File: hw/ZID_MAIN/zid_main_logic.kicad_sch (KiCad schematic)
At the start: 84 parts, among them J1 Conn_01x02_Pin_2.54mm, J2 Conn_02x05_2.54mm, J3 Conn_02x05_2.54mm, J4 Conn_02x05_PINHDR_2.54mm, J5 HDR 1x04 Socket, J6 Conn_02x03_Odd_Even, J7 Conn_01x03, M1 WS-RP2040-Zero, SW1 SW_Push, SW2 SW_DIP_x02, U1 74HCT161, U10 74FCT2245, U11 SST39SF010, U12 AS7C1024B-10J, U13 74FCT541C, U14 74AHCT244, U15 74FCT257T, U16 74HCT166, U17 74HCT166, U18 74LVC245, U19 74LVC125AS, U2 74FCT541C, U20 24LC32, U21 ATF1504AS-44T, U22 74AHCT1G125, U23 74LVC273, U25 74LVC2G04, U26 74AHCT1G14, U3 74FCT541C, U4 MIC2775, U5 OSC-20MHz, U6 Z80 C20MHz-PLCC, U7 ATF1508AS, U8 74FCT2245, U9 74FCT2245

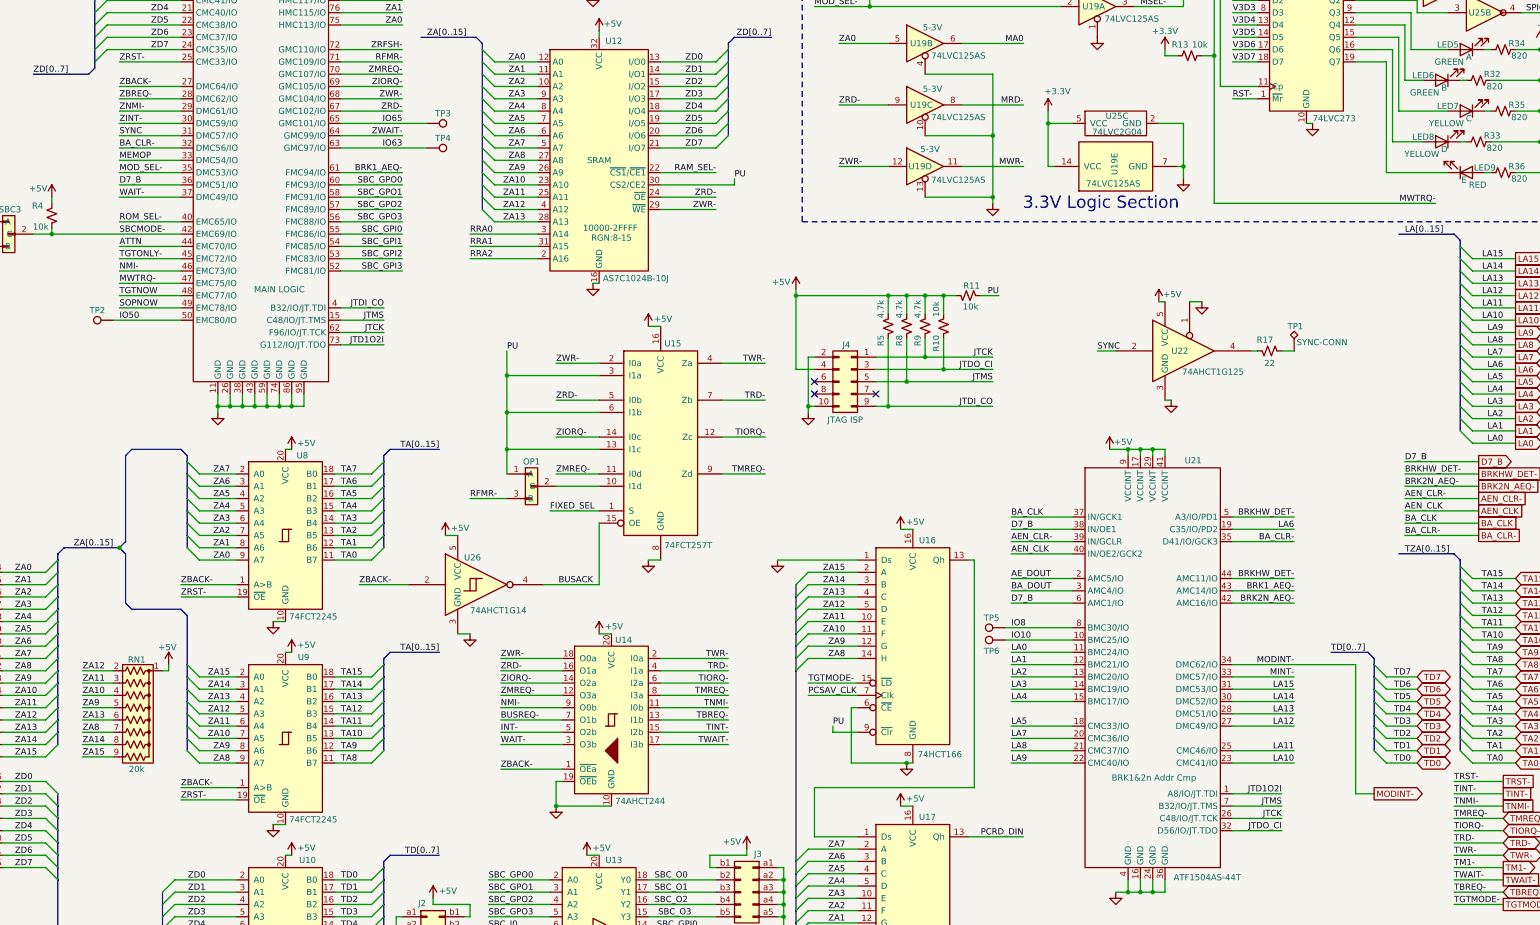
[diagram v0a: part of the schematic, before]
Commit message: BP-EXP: 1 board only. PLCC-DIP: Adapter form.
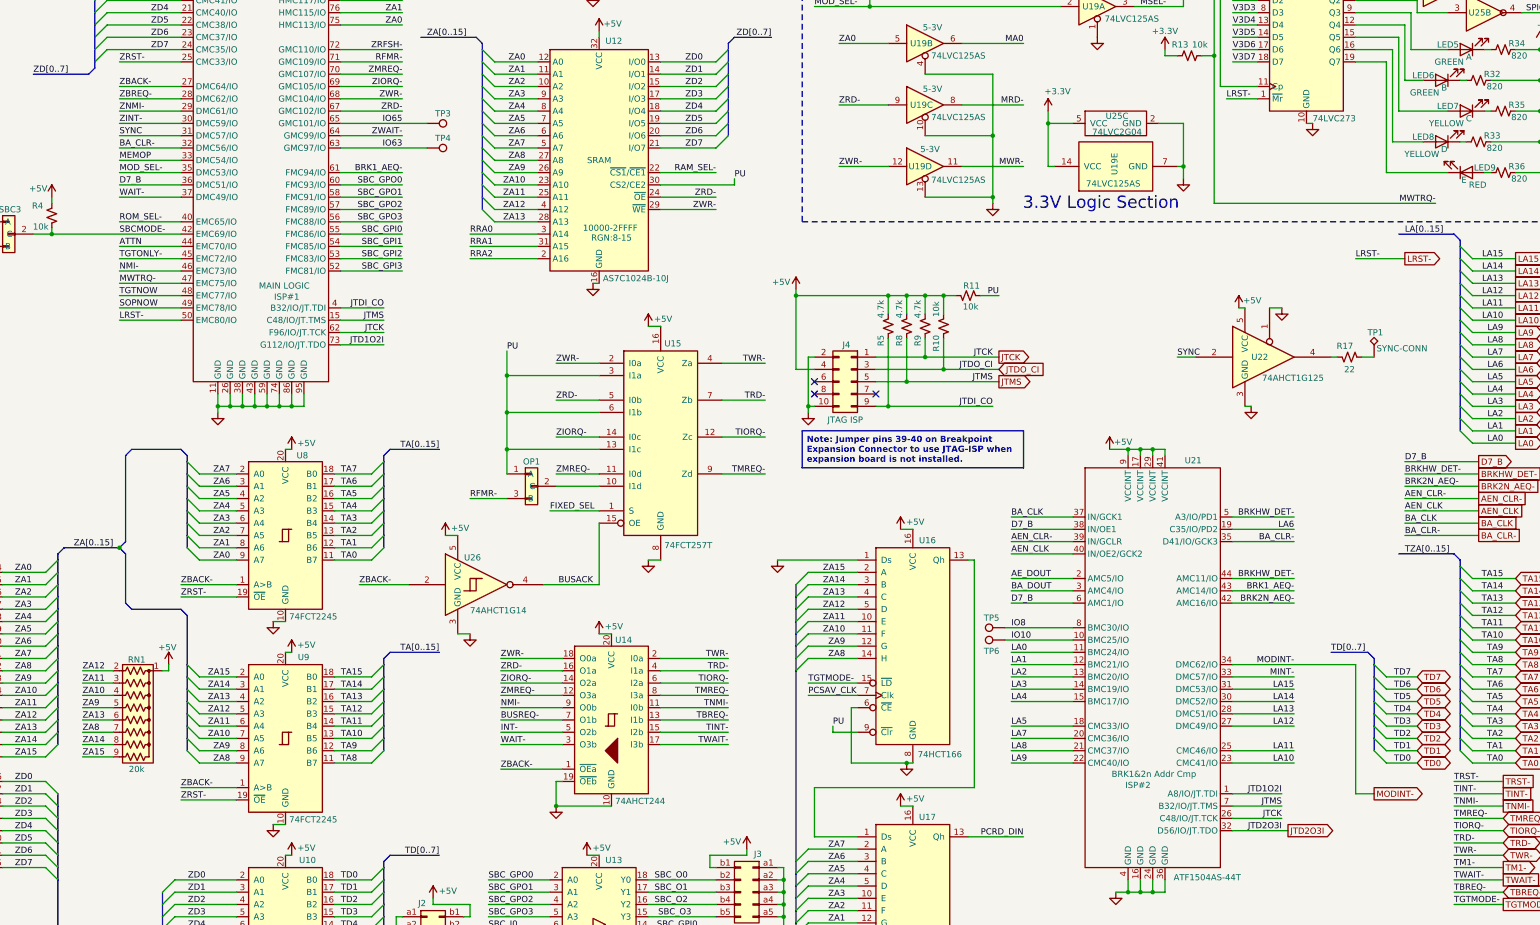
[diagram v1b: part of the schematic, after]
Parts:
- removed TP2: TestPoint, Connector_PinHeader_2.54mm:PinHeader_1x01_P2.54mm_Vertical, symbol Connector:TestPoint
- U21: ISP_CN (none) -> ISP#2
- U7: ISP_CN (none) -> ISP#1
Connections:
- net JTDO_CI: no longer U21.32 (D56/IO/JT.TDO)
- net RST-: no longer U23.1 (~{Mr})
- net IO50 renamed LRST-
- net LRST-: now also U23.1 (~{Mr})
- new net JTD2O3I: U21.32 (D56/IO/JT.TDO)
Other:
- moved on the sheet: R17, TP1, U22

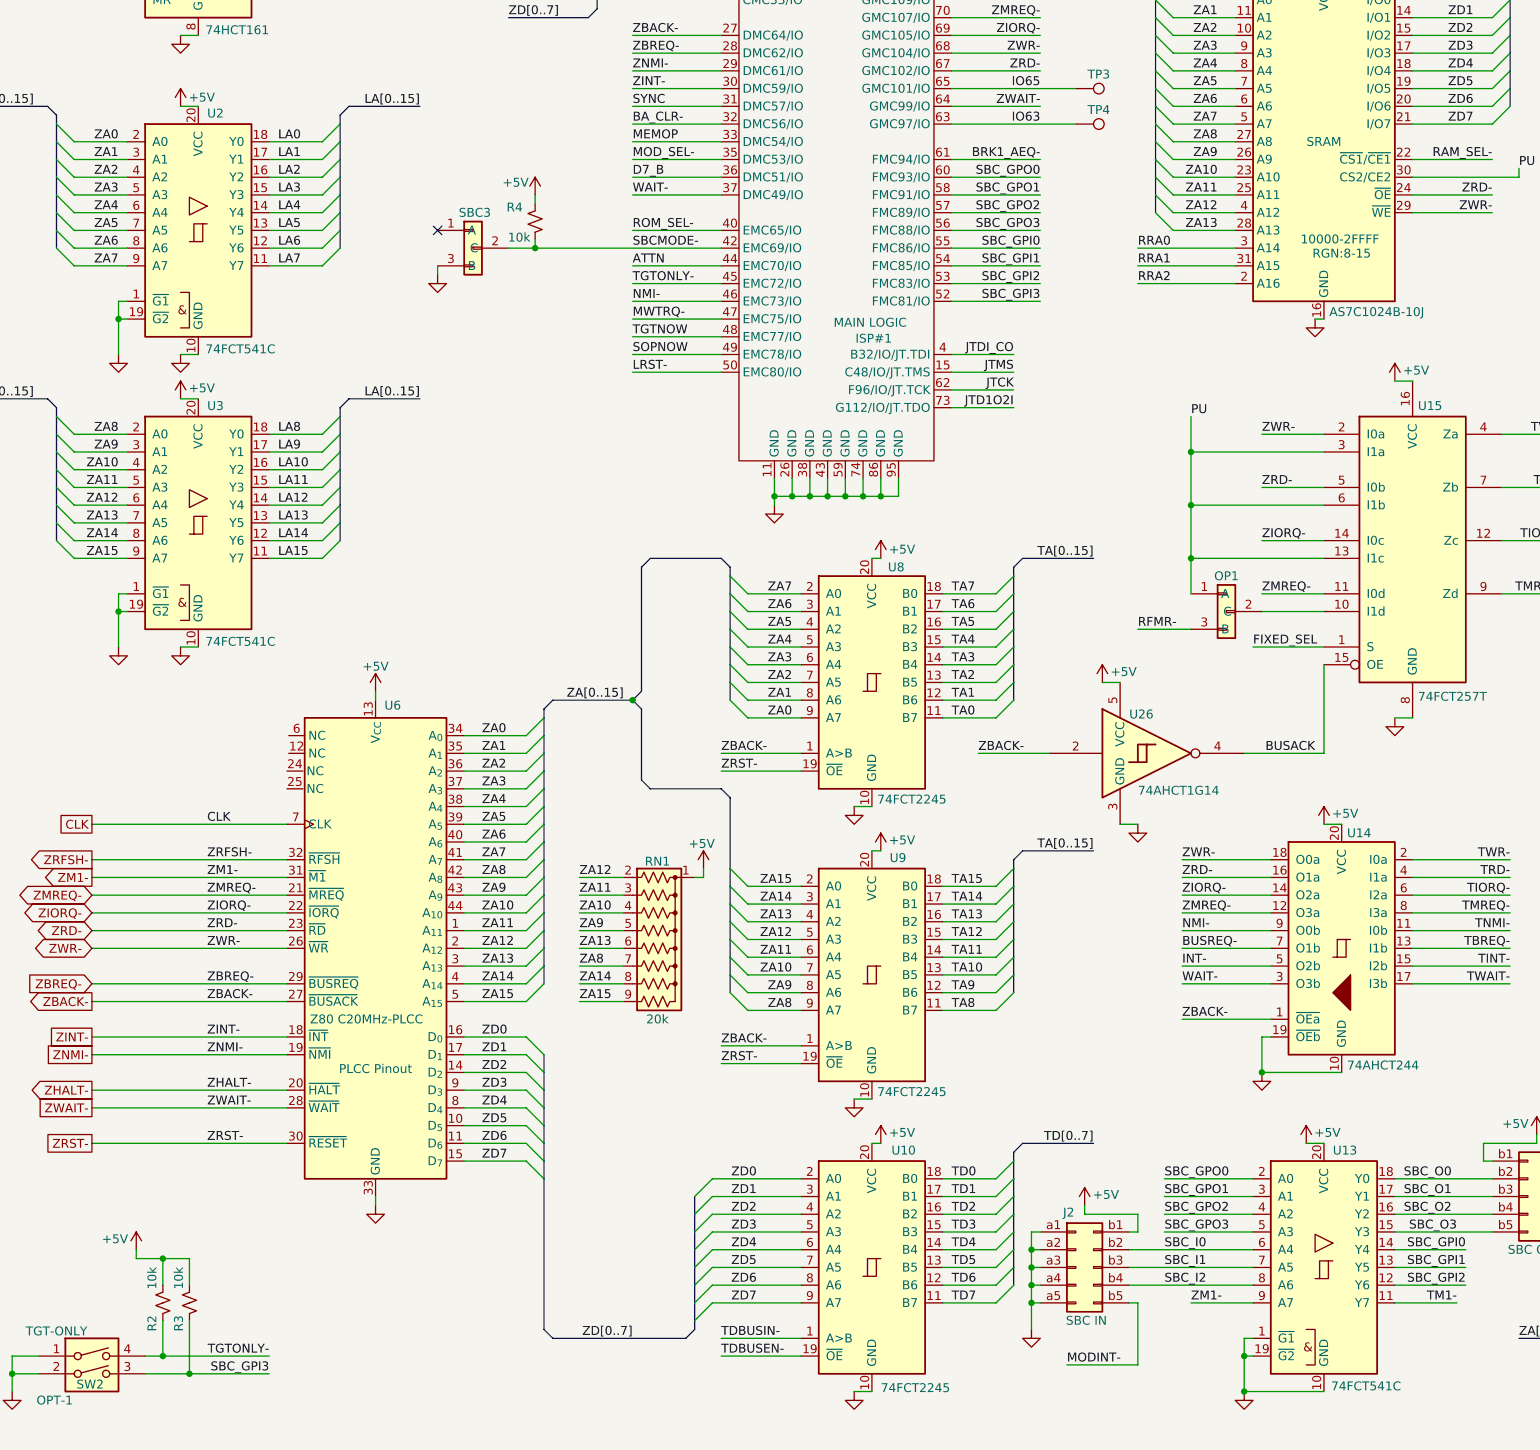
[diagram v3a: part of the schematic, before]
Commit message: 74FCT541 to 74FCT2245. Move GND around CLK on ZID-POD connector
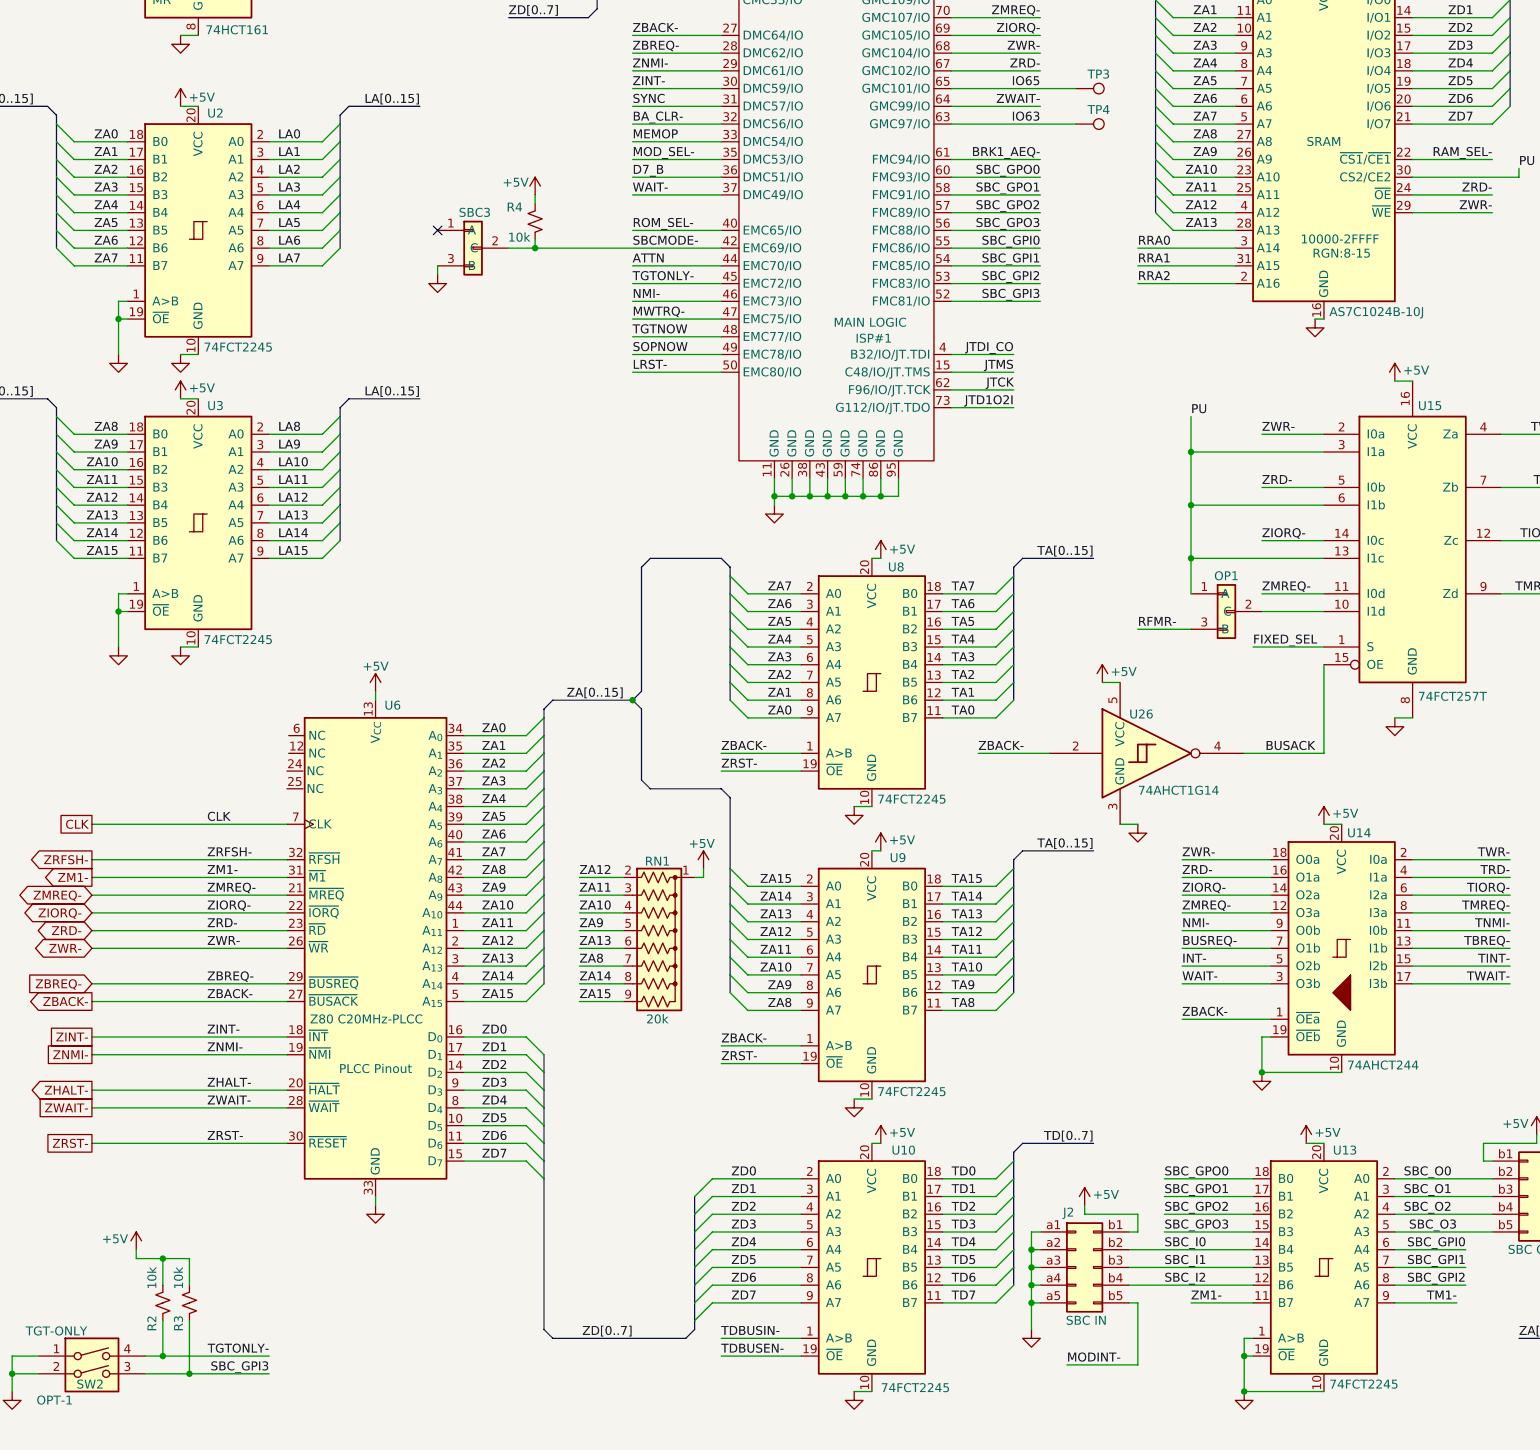
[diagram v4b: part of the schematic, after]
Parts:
- removed U13, U2, U3: 74FCT541C, Package_SO:SOIC-20W_7.5x12.8mm_P1.27mm, symbol AES_Library:74541-AES
- added U3: 74FCT2245, Package_SO:SOIC-20W_7.5x12.8mm_P1.27mm, symbol AES_Library:74245_BA-AES
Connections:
- net +5V: now also U3.20 (VCC)
- net GND: now also U3.1 (A>B), U3.10 (GND), U3.19 (~{OE})
- net LA0: now also U3.2 (A0)
- net LA1: now also U3.3 (A1)
- net LA10: now also U3.4 (A2)
- net LA11: now also U3.5 (A3)
- net LA12: now also U3.6 (A4)
- net LA13: now also U3.7 (A5)
- net LA14: now also U3.8 (A6)
- net LA15: now also U3.9 (A7)
- net LA2: now also U3.4 (A2)
- net LA3: now also U3.5 (A3)
- net LA4: now also U3.6 (A4)
- net LA5: now also U3.7 (A5)
- net LA6: now also U3.8 (A6)
- net LA7: now also U3.9 (A7)
- net LA8: now also U3.2 (A0)
- net LA9: now also U3.3 (A1)
- net SBC_GPI0: now also U3.6 (A4)
- net SBC_GPI1: now also U3.7 (A5)
- net SBC_GPI2: now also U3.8 (A6)
- net SBC_GPO0: now also U3.18 (B0)
- net SBC_GPO1: now also U3.17 (B1)
- net SBC_GPO2: now also U3.16 (B2)
- net SBC_GPO3: now also U3.15 (B3)
- net SBC_I0: now also U3.14 (B4)
- net SBC_I1: now also U3.13 (B5)
- net SBC_I2: now also U3.12 (B6)
- net SBC_O0: now also U3.2 (A0)
- net SBC_O1: now also U3.3 (A1)
- net SBC_O2: now also U3.4 (A2)
- net SBC_O3: now also U3.5 (A3)
- net TM1-: now also U3.9 (A7)
- net ZA0: now also U3.18 (B0)
- net ZA1: now also U3.17 (B1)
- net ZA10: now also U3.16 (B2)
- net ZA11: now also U3.15 (B3)
- net ZA12: now also U3.14 (B4)
- net ZA13: now also U3.13 (B5)
- net ZA14: now also U3.12 (B6)
- net ZA15: now also U3.11 (B7)
- net ZA2: now also U3.16 (B2)
- net ZA3: now also U3.15 (B3)
- net ZA4: now also U3.14 (B4)
- net ZA5: now also U3.13 (B5)
- net ZA6: now also U3.12 (B6)
- net ZA7: now also U3.11 (B7)
- net ZA8: now also U3.18 (B0)
- net ZA9: now also U3.17 (B1)
- net ZM1-: now also U3.11 (B7)

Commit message: PLD: Work around Microchip negative logic issue. PCB add external break.
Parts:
- removed TP4: TestPoint, Connector_PinHeader_2.54mm:PinHeader_1x01_P2.54mm_Vertical, symbol Connector:TestPoint
- removed U22: 74AHCT1G125, Package_TO_SOT_SMD:SOT-23-5, symbol 74xGxx:74LVC1G125
- added JP?: Jumper_2_Small_Bridged, Connector_PinHeader_2.00mm:PinHeader_1x02_P2.00mm_Vertical, symbol Jumper:Jumper_2_Small_Bridged
- added OP2: AES-Option_A-B, Connector_PinHeader_2.54mm:PinHeader_1x03_P2.54mm_Vertical, symbol AES_Library:AES-Option_A-B_2mm
- added R38, R? (x2): 10k, Resistor_SMD:R_0805_2012Metric, symbol Device:R_Small_US
- added R?: 22, Resistor_SMD:R_0805_2012Metric, symbol Device:R_Small_US
- added TP?: EXT-BRK(low actv), Connector_PinHeader_2.54mm:PinHeader_1x01_P2.54mm_Vertical, symbol Connector:TestPoint_Alt
- added U2, U3: 74FCT2245, Package_SO:SOIC-20W_7.5x12.8mm_P1.27mm, symbol AES_Library:74245_BA-AES
- added U? (x3): 74AHCT2G125, symbol 74xGxx:74LVC2G125
- SBC1: Function SBC 2-3 -> RESET
- renumbered U3 to U13
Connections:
- net +5V: now also R38.1, R?.1, R?.1, U2.20 (VCC), U3.20 (VCC), U?.8 (VCC)
- net GND: now also U2.1 (A>B), U2.10 (GND), U2.19 (~{OE}), U3.1 (A>B), U3.10 (GND), U3.19 (~{OE}), U?.1, U?.4 (GND), U?.7
- net LA0: now also U2.2 (A0); no longer U13.2 (A0)
- net LA1: now also U2.3 (A1); no longer U13.3 (A1)
- net LA10: now also U3.4 (A2); no longer U13.4 (A2)
- net LA11: now also U3.5 (A3); no longer U13.5 (A3)
- net LA12: now also U3.6 (A4); no longer U13.6 (A4)
- net LA13: now also U3.7 (A5); no longer U13.7 (A5)
- net LA14: now also U3.8 (A6); no longer U13.8 (A6)
- net LA15: now also U3.9 (A7); no longer U13.9 (A7)
- net LA2: now also U2.4 (A2); no longer U13.4 (A2)
- net LA3: now also U2.5 (A3); no longer U13.5 (A3)
- net LA4: now also U2.6 (A4); no longer U13.6 (A4)
- net LA5: now also U2.7 (A5); no longer U13.7 (A5)
- net LA6: now also U2.8 (A6); no longer U13.8 (A6)
- net LA7: now also U2.9 (A7); no longer U13.9 (A7)
- net LA8: now also U3.2 (A0); no longer U13.2 (A0)
- net LA9: now also U3.3 (A1); no longer U13.3 (A1)
- net SYNC: now also U?.2
- net ZA0: now also U2.18 (B0); no longer U13.18 (B0)
- net ZA1: now also U2.17 (B1); no longer U13.17 (B1)
- net ZA10: now also U3.16 (B2); no longer U13.16 (B2)
- net ZA11: now also U3.15 (B3); no longer U13.15 (B3)
- net ZA12: now also U3.14 (B4); no longer U13.14 (B4)
- net ZA13: now also U3.13 (B5); no longer U13.13 (B5)
- net ZA14: now also U3.12 (B6); no longer U13.12 (B6)
- net ZA15: now also U3.11 (B7); no longer U13.11 (B7)
- net ZA2: now also U2.16 (B2); no longer U13.16 (B2)
- net ZA3: now also U2.15 (B3); no longer U13.15 (B3)
- net ZA4: now also U2.14 (B4); no longer U13.14 (B4)
- net ZA5: now also U2.13 (B5); no longer U13.13 (B5)
- net ZA6: now also U2.12 (B6); no longer U13.12 (B6)
- net ZA7: now also U2.11 (B7); no longer U13.11 (B7)
- net ZA8: now also U3.18 (B0); no longer U13.18 (B0)
- net ZA9: now also U3.17 (B1); no longer U13.17 (B1)
- net ZRST-: now also JP?.1 (A); no longer U6.30 (~{RESET})
- net at R17.2: now also U?.6
- net BUSREQ- renamed TBREQB-
- net INT- renamed TINTB-
- net IO63 renamed EXTBRK-
- net EXTBRK-: now also U?.3
- net NMI- renamed TNMIB-
- net WAIT- renamed TWAITB-
- net TWAITB-: now also OP2.1 (A); no longer U7.37 (DMC49/IO)
- new net: R?.1, R?.2, TP?.1
- new net: JP?.2 (B), R?.2, U6.30 (~{RESET})
- new net: OP2.3 (B), R38.2
- new net: R?.2, U?.5
- new net TWAITRQ-: OP2.2 (C), U7.37 (DMC49/IO)
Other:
- moved on the sheet: C1, J4, JP4, R10, R11, R12, R17, R5, R8, R9, TP1
